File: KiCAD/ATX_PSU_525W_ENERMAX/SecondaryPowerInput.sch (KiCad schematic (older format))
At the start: 16 parts, among them J1 Molex: 0039281243, J2 Molex: 0039281243, J3 Molex: 0039281243, Q3 Q_NMOS_DGS

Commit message: protection changes
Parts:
- removed DZ001: D_Zener, symbol Device:D_Zener
- added DZ1: D_Zener, symbol Device:D_Zener
- added Q1, Q3: Q_NMOS_DGS, Package_TO_SOT_THT:TO-220-3_Vertical, symbol Device:Q_NMOS_GDS
- Q2: renamed from Q3; symbol Device:Q_NMOS_DGS -> Device:Q_NMOS_GDS
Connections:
- wire segments 90 -> 115
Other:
- moved on the sheet: D2, D3, DZ002, DZ003, F2, F3, J2, J3, R2, R3

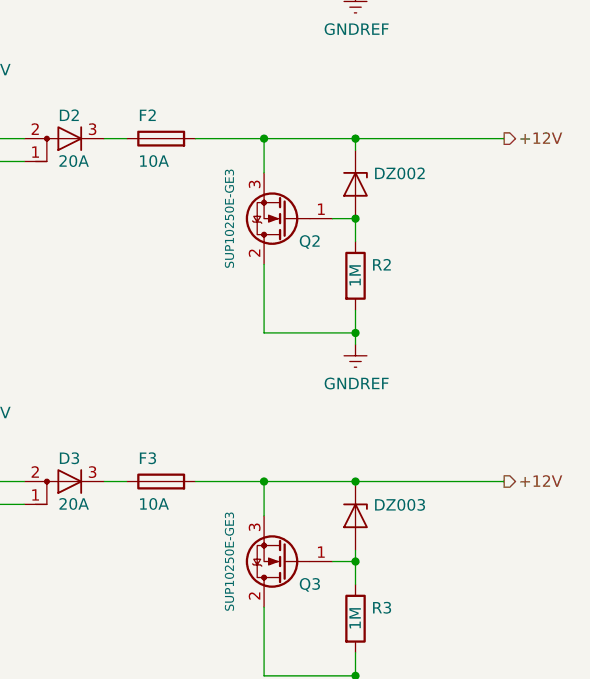
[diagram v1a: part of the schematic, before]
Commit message: moved all sub schematics to base schematic sheet due to minor complexity
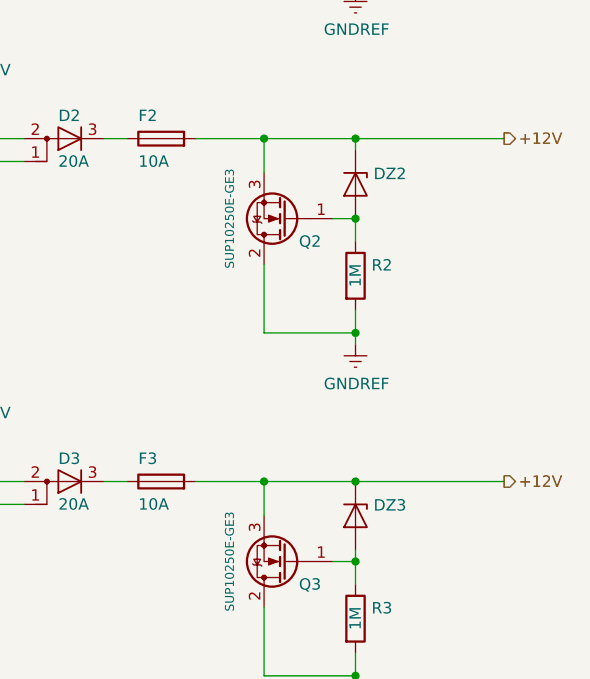
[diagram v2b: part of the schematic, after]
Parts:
- renumbered DZ002 to DZ2, DZ003 to DZ3
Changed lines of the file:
@@
 P 4500 4900
 AR Path="/5E1C8F54" Ref="DZ?"  Part="1"
-AR Path="/5E13FF9B/5E1C8F54" Ref="DZ003"  Part="1"
-F 0 "DZ003" V 4454 4979 50  0000 L CNN
+AR Path="/5E13FF9B/5E1C8F54" Ref="DZ3"  Part="1"
+F 0 "DZ3" V 4454 4979 50  0000 L CNN
 F 1 "D_Zener" V 4545 4979 50  0001 L CNN
 F 2 "" H 4500 4900 50  0001 C CNN
@@
 P 4500 3450
 AR Path="/5E1C8F4E" Ref="DZ?"  Part="1"
-AR Path="/5E13FF9B/5E1C8F4E" Ref="DZ002"  Part="1"
-F 0 "DZ002" V 4454 3529 50  0000 L CNN
+AR Path="/5E13FF9B/5E1C8F4E" Ref="DZ2"  Part="1"
+F 0 "DZ2" V 4454 3529 50  0000 L CNN
 F 1 "D_Zener" V 4545 3529 50  0001 L CNN
 F 2 "" H 4500 3450 50  0001 C CNN
@@
 $EndComp
 $Comp
-L power:GNDREF #PWR?
+L power:GNDREF #PWR0103
 U 1 1 61694CA0
 P 4500 2600
-F 0 "#PWR?" H 4500 2350 50  0001 C CNN
+F 0 "#PWR0103" H 4500 2350 50  0001 C CNN
 F 1 "GNDREF" H 4505 2427 50  0000 C CNN
 F 2 "" H 4500 2600 50  0001 C CNN
@@
 	2050 3450 2050 3550
 $Comp
-L power:+12V #PWR?
+L power:+12V #PWR0106
 U 1 1 6168825C
 P 2900 1550
-F 0 "#PWR?" H 2900 1400 50  0001 C CNN
+F 0 "#PWR0106" H 2900 1400 50  0001 C CNN
 F 1 "+12V" H 2800 1700 50  0000 L CNN
 F 2 "" H 2900 1550 50  0001 C CNN
